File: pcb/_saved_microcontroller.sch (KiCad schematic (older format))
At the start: 14 parts, among them J401 JSTA-4, P401 SWD, P402 USB_OTG, SW401 SPST, U401 STM32F072CBT6

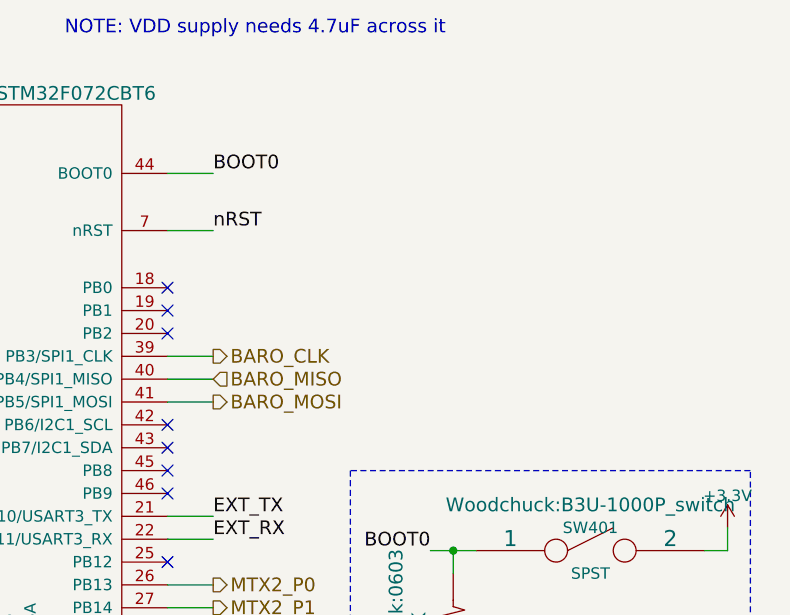
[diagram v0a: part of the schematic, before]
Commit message: Add 24AA01 EEPROM and add agg-kicad library
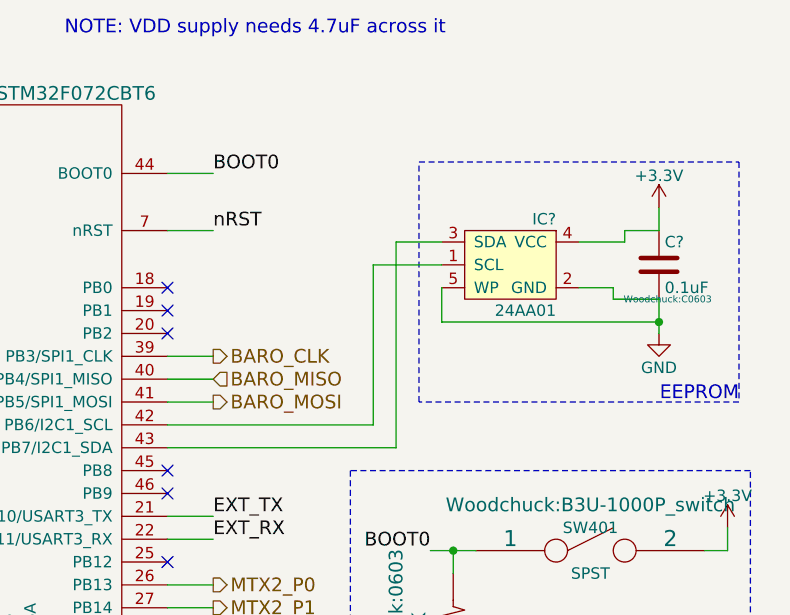
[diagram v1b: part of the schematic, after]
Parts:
- added C?: 0.1uF, Woodchuck:C0603, symbol C
- added IC?: 24AA01, agg:SOT-23-5, symbol 24AA01
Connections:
- net +3V3: now also C?.1, IC?.4 (VCC)
- net GND: now also C?.2, IC?.2 (GND), IC?.5 (WP)
- net at U401.42 (PB6/I2C1_SCL): now also IC?.1 (SCL)
- net at U401.43 (PB7/I2C1_SDA): now also IC?.3 (SDA)
- no-connect marks 23 -> 21
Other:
- note added: "EEPROM"
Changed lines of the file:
@@
 LIBS:sma
 LIBS:cga0402mlc-12g
+LIBS:agg-kicad
 LIBS:woodchuck-cache
 EELAYER 25 0
@@
 NoConn ~ 6700 3700
 NoConn ~ 6700 3800
-NoConn ~ 6700 4200
-NoConn ~ 6700 4300
 NoConn ~ 6700 4400
 NoConn ~ 6700 4500
@@
 Text HLabel 6900 4900 2    60   Output ~ 0
 MTX2_P0
+$Comp
+L 24AA01 IC?
+U 1 1 56BF54E5
+P 8200 3500
+F 0 "IC?" H 8000 3700 50  0000 L CNN
+F 1 "24AA01" H 8000 3300 50  0000 L CNN
+F 2 "agg:SOT-23-5" H 8000 3200 50  0001 L CNN
+F 3 "http://ww1.microchip.com/downloads/en/DeviceDoc/21711c.pdf" H 8000 3100 50  0001 L CNN
+F 4 "1331269" H 8000 3000 50  0001 L CNN "Farnell"
+	1    8200 3500
+	-1   0    0    -1
+$EndComp
+$Comp
+L C C?
+U 1 1 56BF5C75
+P 8850 3500
+F 0 "C?" H 8875 3600 50  0000 L CNN
+F 1 "0.1uF" H 8875 3400 50  0000 L CNN
+F 2 "Woodchuck:C0603" H 8888 3350 30  0000 C CNN
+F 3 "" H 8850 3500 60  0000 C CNN
+F 4 "Value" H 8850 3500 60  0001 C CNN "Digikey"
+F 5 "9406140" H 8850 3500 60  0001 C CNN "Farnell"
+F 6 "Value" H 8850 3500 60  0001 C CNN "Fieldname"
+	1    8850 3500
+	1    0    0    -1
+$EndComp
+Wire Wire Line
+	8500 3400 8700 3400
+Wire Wire Line
+	8700 3400 8700 3350
+Wire Wire Line
+	8700 3350 8850 3350
+Wire Wire Line
+	8500 3600 8650 3600
+Wire Wire Line
+	8650 3600 8650 3650
+Wire Wire Line
+	8650 3650 8850 3650
+$Comp
+L GND #PWR?
+U 1 1 56BF61FD
+P 8850 3800
+F 0 "#PWR?" H 8850 3550 50  0001 C CNN
+F 1 "GND" H 8850 3650 50  0000 C CNN
+F 2 "" H 8850 3800 60  0000 C CNN
+F 3 "" H 8850 3800 60  0000 C CNN
+	1    8850 3800
+	1    0    0    -1
+$EndComp
+Wire Wire Line
+	8850 3650 8850 3800
+$Comp
+L +3.3V #PWR?
+U 1 1 56BF6515
+P 8850 3250
+F 0 "#PWR?" H 8850 3100 50  0001 C CNN
+F 1 "+3.3V" H 8850 3390 50  0000 C CNN
+F 2 "" H 8850 3250 50  0000 C CNN
+F 3 "" H 8850 3250 50  0000 C CNN
+	1    8850 3250
+	1    0    0    -1
+$EndComp
+Wire Wire Line
+	8850 3350 8850 3250
+Wire Wire Line
+	8850 3750 7900 3750
+Wire Wire Line
+	7900 3750 7900 3600
+Connection ~ 8850 3750
+Wire Wire Line
+	6700 4200 7600 4200
+Wire Wire Line
+	7600 4200 7600 3500
+Wire Wire Line
+	7600 3500 7900 3500
+Wire Wire Line
+	7900 3400 7700 3400
+Wire Wire Line
+	7700 3400 7700 4300
+Wire Wire Line
+	7700 4300 6700 4300
+Wire Notes Line
+	7800 3050 9200 3050
+Wire Notes Line
+	9200 3050 9200 4100
+Wire Notes Line
+	9200 4100 7800 4100
+Wire Notes Line
+	7800 4100 7800 3050
+Text Notes 9200 4100 2    60   ~ 0
+EEPROM
 $EndSCHEMATC
